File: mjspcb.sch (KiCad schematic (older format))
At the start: 50 parts, among them P1 Batteries, P10 Lipo, P11 grove i2c, P12 grove analog, P13 grove analog, P14 HPMA115S0-XXX, P15 piggyback, P2 serial breakout, P3 I2C breakout, P4 GPS, P5 piezo, P6 BPW34, P7 electrodes, P8 perfboard breakout, P9 reset, Q1 STU60N3LH5, Q2 STU60N3LH5, U1 ATMEGA328P, U2 RFM95W, U3 MCP1700-3302

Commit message: Replace with MJS2020-PROTO2 redesign
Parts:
- removed AE1: Antenna, Connector_PinHeader_2.54mm:PinHeader_1x01_P2.54mm_Vertical, symbol Device:Antenna
- removed C2, C4: 100u, Capacitor_THT:CP_Radial_D5.0mm_P2.00mm, symbol Device:CP
- removed D1: LED, LED_THT:LED_D3.0mm, symbol Device:LED
- removed DC1: 2.7 - 6.0 VDC, Connector_BarrelJack:BarrelJack_Wuerth_6941xx301002, symbol Connector:Barrel_Jack_Switch
- removed H4: MountingHole, MountingHole:MountingHole_3mm, symbol Mechanical:MountingHole
- removed JP1: power select, Connector_PinHeader_2.54mm:PinHeader_1x03_P2.54mm_Vertical, symbol Jumper:Jumper_3_Open
- removed JP2: V1, meetjestad:SolderJumper-3_P1.3mm_Bridged12_RoundedPad1.0x1.5mm_NumberLabels, symbol Jumper:SolderJumper_3_Bridged12
- removed JP3: V2, meetjestad:SolderJumper-3_P1.3mm_Bridged12_RoundedPad1.0x1.5mm_NumberLabels, symbol Jumper:SolderJumper_3_Bridged12
- removed LOGO1: Open source hardware, Symbol:OSHW-Logo_5.7x6mm_SilkScreen, symbol Graphic:Logo_Open_Hardware_Small
- removed LOGO2: MJS Logo, meetjestad:mjs, symbol Graphic:Logo_Open_Hardware_Small
- removed P1: Batteries, Battery:BatteryHolder_Keystone_2479_3xAAA, symbol Connector_Generic:Conn_01x02
- removed P10: Lipo, Connector_JST:JST_PH_S2B-PH-K_1x02_P2.00mm_Horizontal, symbol Connector_Generic:Conn_01x02
- removed P11: grove i2c, Connector:NS-Tech_Grove_1x04_P2mm_Vertical, symbol Connector_Generic:Conn_01x04
- removed P12: grove analog, meetjestad:NS-Tech_Grove_1x04_P2mm_P2.54mm_Vertical, symbol Connector_Generic:Conn_01x04
- removed P13: grove analog, meetjestad:NS-Tech_Grove_1x04_P2mm_P2.54mm_Vertical_Alternative, symbol Connector_Generic:Conn_01x04
- removed P14: HPMA115S0-XXX, Connector_Molex:Molex_PicoBlade_53047-0810_1x08_P1.25mm_Vertical, symbol Connector_Generic:Conn_01x08
- removed P15: piggyback, Connector_PinHeader_2.54mm:PinHeader_1x12_P2.54mm_Vertical, symbol Connector_Generic:Conn_01x12
- removed P2: serial breakout, Connector_PinHeader_2.54mm:PinHeader_1x06_P2.54mm_Vertical, symbol Connector_Generic:Conn_01x06
- removed P3: I2C breakout, meetjestad:Molex_KK-254_44812-0004_1x04_P2.54mm_Vertical, symbol Connector_Generic:Conn_01x04
- removed P4: GPS, Connector_JST:JST_PH_S3B-PH-K_1x03_P2.00mm_Horizontal, symbol Connector_Generic:Conn_01x03
- removed P5: piezo, Connector_Molex:Molex_KK-254_AE-6410-02A_1x02_P2.54mm_Vertical, symbol Connector_Generic:Conn_01x02
- removed P6: BPW34, Connector_Molex:Molex_KK-254_AE-6410-02A_1x02_P2.54mm_Vertical, symbol Connector_Generic:Conn_01x02
- removed P7: electrodes, Connector_Molex:Molex_KK-254_AE-6410-02A_1x02_P2.54mm_Vertical, symbol Connector_Generic:Conn_01x02
- removed P8: perfboard breakout, Connector_PinHeader_2.54mm:PinHeader_1x11_P2.54mm_Vertical, symbol Connector_Generic:Conn_01x11
- removed P9: reset, Connector_PinHeader_2.54mm:PinHeader_1x02_P2.54mm_Vertical, symbol Connector_Generic:Conn_01x02
- removed Q1, Q2: STU60N3LH5, Package_TO_SOT_THT:TO-251-3_Vertical, symbol Device:Q_NMOS_GDS
- removed R1: 10k, Resistor_THT:R_Axial_DIN0207_L6.3mm_D2.5mm_P10.16mm_Horizontal, symbol Device:R
- removed U1: ATMEGA328P, Package_DIP:DIP-28_W7.62mm_Socket, symbol MCU_Microchip_ATmega:ATmega328P-PU
- removed U2: RFM95W, RF_Module:HOPERF_RFM9XW_SMD, symbol RF_AM_FM:RFM95W-868S2
- removed U3: MCP1700-3302, Package_TO_SOT_THT:TO-92_Inline, symbol Regulator_Linear:MCP1700-3302E_TO92
- added C10, C11, C12, C13, C17, C25, C32, C33, C34, C35, C36, C37, C4, C6, C9: 100nF, Capacitor_SMD:C_0805_2012Metric_Pad1.15x1.40mm_HandSolder, symbol Device:C
- added C14, C15, C19, C20, C21, C23, C24, C26, C31, C7: 1uF, Capacitor_SMD:C_0805_2012Metric_Pad1.15x1.40mm_HandSolder, symbol Device:C
- added C16, C18, C22, C27, C28, C29, C30, C8: 4.7uF, Capacitor_SMD:C_0805_2012Metric_Pad1.15x1.40mm_HandSolder, symbol Device:C
- added C2: 12.5pF, Capacitor_SMD:C_0805_2012Metric_Pad1.15x1.40mm_HandSolder, symbol Device:C
- added D1, D2, D3: MBR120VLSFT3G, meetjestad:Diode_SMD-SOD_123, symbol mjspcb-rescue:DIODE-pspice-POC_Rev01-rescue
- added D4: 6,2V, meetjestad:D_SOD-123, symbol Device:D_Zener
- added FB1, FB2, FB3: Ferrite_Bead, Resistor_SMD:R_0805_2012Metric_Pad1.15x1.40mm_HandSolder, symbol mjspcb-rescue:Ferrite_Bead-Device-POC_Rev01-rescue
- added FID1, FID2, FID3: Fiducial, Fiducial:Fiducial_0.5mm_Mask1mm, symbol Mechanical:Fiducial
- added J1: FTDI, Connector_PinHeader_2.54mm:PinHeader_1x06_P2.54mm_Vertical, symbol Connector:Conn_01x06_Male
- added J10: Analog, meetjestad:Grove_4pin&Header_4pin, symbol Connector_Generic:Conn_01x04
- added J11: BOOT0, Connector_PinHeader_2.54mm:PinHeader_1x02_P2.54mm_Vertical, symbol Connector:Conn_01x02_Male
- added J12: Tag connect, meetjestad:Tag connect, symbol Connector:Conn_01x06_Male
- added J13: Conn_Coaxial, meetjestad:SMA connector edge mount, symbol Connector:Conn_Coaxial
- added J14: Lithium Ion, meetjestad:BatteryHolder_18650-PC2, symbol Connector:Conn_01x02_Male
- added J15: Temp/Hum, meetjestad:Grove_4pin&Header_4pin, symbol mjspcb-rescue:Conn_01x04_Male-Connector-POC_Rev01-rescue
- added J16: BPW34, Connector_PinHeader_2.54mm:PinHeader_1x02_P2.54mm_Vertical, symbol Connector:Conn_01x02_Male
- added J17: USB_C_connector, 632723300011_Eagle_WR-USB_rev20b:632723100011, symbol meetjestad:USB_C_connector
- added J18: I2C 3V_perm, meetjestad:Grove_4pin&Header_4pin, symbol Connector_Generic:Conn_01x04
- added J19: I2C 5V_SW, meetjestad:Grove_4pin&Header_4pin, symbol Connector_Generic:Conn_01x04
- added J20: Multi, meetjestad:Grove_4pin&Header_4pin, symbol Connector_Generic:Conn_01x04
- added J3: Prototype header, Connector_PinSocket_2.54mm:PinSocket_1x15_P2.54mm_Vertical, symbol Connector:Conn_01x15_Female
- added J4: Oled, Connector_PinSocket_2.54mm:PinSocket_1x04_P2.54mm_Vertical, symbol mjspcb-rescue:Conn_01x04_Male-Connector-POC_Rev01-rescue
- added J5: Conn_01x02_Male, meetjestad:Battery__holder, symbol Connector:Conn_01x02_Male
- added J6: Solar, Connector_PinHeader_2.54mm:PinHeader_1x02_P2.54mm_Vertical, symbol Connector:Conn_01x02_Male
- added J7: Particulate matter, meetjestad:B5B-ZR, symbol Connector:Conn_01x05_Female
- added J8: Prototype power, Connector_PinSocket_2.54mm:PinSocket_1x06_P2.54mm_Vertical, symbol Connector:Conn_01x06_Female
- added J9: Prototype GND, Connector_PinSocket_2.54mm:PinSocket_1x06_P2.54mm_Vertical, symbol Connector:Conn_01x06_Female
- added L1: 4.7uH, Resistor_SMD:R_0805_2012Metric_Pad1.15x1.40mm_HandSolder, symbol mjspcb-rescue:L-Device-POC_Rev01-rescue
- added LED1: JT-S3030_RGB_LED, meetjestad:JT-S3030_RGB_LED, symbol meetjestad:JT-S3030_RGB_LED
- added Logo_kitt1: Logo_Open_Hardware_Small, meetjestad:Kitt_logo, symbol Graphic:Logo_Open_Hardware_Small
- added Logo_mjs1: Logo_Open_Hardware_Small, meetjestad:mjs_logo, symbol Graphic:Logo_Open_Hardware_Small
- added Logo_mjs2: Logo_Open_Hardware_Small, Symbol:OSHW-Logo2_7.3x6mm_SilkScreen, symbol Graphic:Logo_Open_Hardware_Small
- added PSU1, PSU3, PSU4: TPS7A02, Package_TO_SOT_SMD:SOT-23-5_HandSoldering, symbol mjspcb-rescue:TPS7A02-meetjestad-POC_Rev01-rescue
- added PSU2: XC9140A501MR-G, Package_TO_SOT_SMD:SOT-23-5_HandSoldering, symbol mjspcb-rescue:XC9140A501MR-G-meetjestad-POC_Rev01-rescue
- added Q1, Q2: DMP2035U-7, Package_TO_SOT_SMD:SOT-23, symbol Transistor_FET:DMG2301L
- added R1: 1k, Resistor_SMD:R_0805_2012Metric_Pad1.15x1.40mm_HandSolder, symbol mjspcb-rescue:R-Device-POC_Rev01-rescue
- added R14, R16, R25: 100k, Resistor_SMD:R_0805_2012Metric_Pad1.15x1.40mm_HandSolder, symbol Device:R
- added R15, R20, R21, R28, R29, R30, R31, R32, R33, R39, R40, R43, R44, R45, R46: 10k, Resistor_SMD:R_0805_2012Metric_Pad1.15x1.40mm_HandSolder, symbol Device:R
- added R17, R18, R34, R35, R36, R41, R42: 1k, Resistor_SMD:R_0805_2012Metric_Pad1.15x1.40mm_HandSolder, symbol Device:R
- added R19, R22, R23, R24, R26, R27: 1M, Resistor_SMD:R_0805_2012Metric_Pad1.15x1.40mm_HandSolder, symbol Device:R
- added R37, R38: 100, Resistor_SMD:R_0805_2012Metric_Pad1.15x1.40mm_HandSolder, symbol Device:R
- added SP1, SP2, SP3, SP4, SP5, SP6: SolderJumper_2_Open, Jumper:SolderJumper-2_P1.3mm_Open_TrianglePad1.0x1.5mm, symbol Jumper:SolderJumper_2_Open
- added SW1, SW2: SW_Push, Button_Switch_THT:SW_PUSH_6mm, symbol Switch:SW_Push
- added TP1, TP2, TP3, TP4: TestPoint_Small, TestPoint:TestPoint_Pad_D1.0mm, symbol mjspcb-rescue:TestPoint_Small-Connector-mjspcb-rescue
- added TP5: Sticker field, meetjestad:Sticker field, symbol Connector:TestPoint_Small
- added TP6: Flash OK, meetjestad:Flash OK, symbol Connector:TestPoint_Small
- added TP7: Test OK, meetjestad:Test OK, symbol Connector:TestPoint_Small
- added U1: USBLC-2SC6, Package_TO_SOT_SMD:SOT-23-6_Handsoldering, symbol meetjestad:USBLC-2SC6
- added U2: LoRa_1262_G-NiceRF, meetjestad:LoRa_1262_G-NiceRF, symbol mjspcb-rescue:LoRa_1262_G-NiceRF-meetjestad-POC_Rev01-rescue
- added U3: GPS, meetjestad:GPS_ublox-SAM-M8Q, symbol mjspcb-rescue:ublox_SAM-M8Q-RF_GPS-POC_Rev01-rescue
- added U4: PrototypeGrid, meetjestad:Prototype grid, symbol meetjestad:PrototypeGrid
- added U5: STM32L072RBTx-meetjestad, meetjestad:STM32F072_LQFP-64, symbol mjspcb-rescue:STM32L072RBTx-meetjestad-POC_Rev01-rescue
- added U6: MCP73831, Package_TO_SOT_SMD:SOT-23-5_HandSoldering, symbol meetjestad:MCP73831
- added Y1: 32kHz, Resistor_SMD:R_0805_2012Metric_Pad1.15x1.40mm_HandSolder, symbol mjspcb-rescue:Crystal-Device-POC_Rev01-rescue
- C1: value 100n -> 12.5pF; footprint Capacitor_THT:C_Disc_D3.0mm_W1.6mm_P2.50mm -> Capacitor_SMD:C_0805_2012Metric_Pad1.15x1.40mm_HandSolder
- C3, C5: value 100n -> 100nF; footprint Capacitor_THT:C_Disc_D3.0mm_W1.6mm_P2.50mm -> Capacitor_SMD:C_0805_2012Metric_Pad1.15x1.40mm_HandSolder
- H1, H2, H3: footprint MountingHole:MountingHole_3mm -> meetjestad:Mounting_hole
- R10: value 1k -> 100k; footprint Resistor_THT:R_Axial_DIN0207_L6.3mm_D2.5mm_P10.16mm_Horizontal -> Resistor_SMD:R_0805_2012Metric_Pad1.15x1.40mm_HandSolder
- R11: value 10k -> 100k; footprint Resistor_THT:R_Axial_DIN0207_L6.3mm_D2.5mm_P10.16mm_Horizontal -> Resistor_SMD:R_0805_2012Metric_Pad1.15x1.40mm_HandSolder
- R12: value 100k -> 1k; footprint Resistor_THT:R_Axial_DIN0207_L6.3mm_D2.5mm_P10.16mm_Horizontal -> Resistor_SMD:R_0805_2012Metric_Pad1.15x1.40mm_HandSolder
- R13, R6, R7: footprint Resistor_THT:R_Axial_DIN0207_L6.3mm_D2.5mm_P10.16mm_Horizontal -> Resistor_SMD:R_0805_2012Metric_Pad1.15x1.40mm_HandSolder
- R2, R9: value 10k -> 1k; footprint Resistor_THT:R_Axial_DIN0207_L6.3mm_D2.5mm_P10.16mm_Horizontal -> Resistor_SMD:R_0805_2012Metric_Pad1.15x1.40mm_HandSolder
- R3, R4, R5, R8: value 1k -> 10k; footprint Resistor_THT:R_Axial_DIN0207_L6.3mm_D2.5mm_P10.16mm_Horizontal -> Resistor_SMD:R_0805_2012Metric_Pad1.15x1.40mm_HandSolder
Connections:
- net labels added: 3V-perm_CPU, 3V-sw_GPS, 3V-sw_sens, 5V-sw, BOOT0, NRST, PA0, PA1, PA10, PA11, PA12, PA13, PA14, PA15, PA2, PA3, PA4, PA5, PA6, PA7, PA8, PA9, PB0, PB1, PB10, PB11, PB12, PB13, PB14, PB15, PB2, PB3, PB4, PB5, PB6, PB7, PB8, PB9, PC0, PC1, PC10, PC11, PC2, PC3, PC4, PC5, PC6, PC7, PC8, PC9, PH0, PH1, Solar, VBUS, Vin
- net labels removed: -BATT, 5V, A0, A1, A2, A3, D10, D2, D3, D4, D5, D6, D7, D8, D9, MISO, MOSI, RST, RXD, SCK, SCL, SDA, SW_GND, TXD, VCC, VIN, X1, X2
- wire segments 203 -> 500
- no-connect marks 8 -> 0
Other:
- note added: "1% precision\n"
- note added: "ADC4"
- note added: "ADC5\n"
- note added: "ADC_IN0 / Dx\n"
- note added: "ADC_IN1 / Dx"
- note added: "ADC_IN4 / DAC_OUT1"
- note added: "ADC_IN5 / DAC_OUT2"
- note added: "ADC_IN8 / VREF_OUT\n"
- note added: "Battery voltage: 0V - 6V\nPC4 Voltage: 0V - 3V"
- note added: "Board ID\n"
- note added: "C1 and C2: High-quality external ceramic capacitors"
- note added: "Ceramic, 10V\n"
- note added: "Charge status\nTri-state logic output\n\n"
- note added: "Close for I2C communication"
- note added: "Crystal: ABS06-32.768KHZ-1-T\n"
- note added: "DNP\n"
- note added: "Dx"
- note added: "GND: I2C, floating: UART"
- note added: "Grove connectoren\n"
- note added: "H: Active\nL: Stand-by\n"
- note added: "I2C 3V_perm sensors"
- note added: "I2C 5V_SW sensors"
- note added: "I2C1_SCL"
- note added: "I2C1_SCL 3V perm\n"
- note added: "I2C1_SDA"
- note added: "I2C1_SDA 3V perm\n"
- note added: "I2C2_SCL"
- note added: "I2C2_SCL 5V_SW"
- note added: "I2C2_SDA"
- note added: "I2C2_SDA 5V_SW"
- note added: "Ireg = 200mA"
- note added: "Logo KITT\n"
- note added: "Logo mjs"
- note added: "Logo open hardware"
- note added: "Microcontroller\n"
- note added: "POWER\n"
- note added: "Prototype\n"
- note added: "SPI1_MISO"
- note added: "SPI1_MOSI 3V perm"
- note added: "SPI1_NSS\n"
- note added: "SPI1_SCK\n"
- note added: "SPI2_MISO / I2C2_SDA / I2S2_MCK"
- note added: "SPI2_MOSI / I2S2_SD"
- note added: "SPI2_NSS / I2C2_SMBA / I2S2_WS\n"
- note added: "SPI2_SCK / I2C2_SCL / I2S2_CK\n"
- note added: "SWCLK\n"
- note added: "SWDIO\n"
- note added: "Sensors"
- note added: "Threshold voltage: -0.7 V\n"
- note added: "USART1_RX"
- note added: "USART1_TX\n"
- note added: "USART2_RX\n"
- note added: "USART2_TX"
- note added: "USB_DM\n"
- note added: "USB_DP\n"
- note added: "Vout = 2V\n"
- note added: "filter\n"
- note added: "ground plane on top layer\n"
- note added: "pair 100 ohm\n"
- note removed: "!! 5V for HPMA !!"
- note removed: "!! 5V for SDS011 !!"
- note removed: "A1 shared with P7"
- note removed: "Air temperature and humidity sensor"
- note removed: "D6/D7 shared with P7"
- note removed: "Disdrometer"
- note removed: "GPS module"
- note removed: "Intended for softserial"
- note removed: "Other sensors"
- note removed: "PAR meter"
- note removed: "Soil moisture sensor"
- note removed: "aquatictechtank.net/viewtopic.php?f=11&t=150"
- note removed: "core schematic"
- note removed: "forum.arduino.cc/index.php?topic=37975"
- note removed: "optional sensors"
- note removed: "power & programming"
- note removed: "rx"
- note removed: "rx/tx viewed from MCU"
- note removed: "standard sensors"
- note removed: "tx"
- note removed: "www.hoperf.nl/RFM95W"
- note removed: "www.sparkfun.com/products/13740"
- note removed: "www.sparkfun.com/products/13763"

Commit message: Update to MJS2020-PROTO3
See CHANGELOG.md for detailed changes.
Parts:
- removed J11: BOOT0, Connector_PinHeader_2.54mm:PinHeader_1x02_P2.54mm_Vertical, symbol Connector:Conn_01x02_Male
- removed J3: Prototype header, Connector_PinSocket_2.54mm:PinSocket_1x15_P2.54mm_Vertical, symbol Connector:Conn_01x15_Female
- removed LED1: JT-S3030_RGB_LED, meetjestad:JT-S3030_RGB_LED, symbol meetjestad:JT-S3030_RGB_LED
- removed R1: 1k, Resistor_SMD:R_0805_2012Metric_Pad1.15x1.40mm_HandSolder, symbol mjspcb-rescue:R-Device-POC_Rev01-rescue
- removed SP3, SP4, SP5, SP6: SolderJumper_2_Open, Jumper:SolderJumper-2_P1.3mm_Open_TrianglePad1.0x1.5mm, symbol Jumper:SolderJumper_2_Open
- removed TP1, TP2, TP3, TP4: TestPoint_Small, TestPoint:TestPoint_Pad_D1.0mm, symbol mjspcb-rescue:TestPoint_Small-Connector-mjspcb-rescue
- added C38, C39, C40: 100nF, Capacitor_SMD:C_0805_2012Metric_Pad1.15x1.40mm_HandSolder, symbol mjspcb-rescue:C-Device-POC_Rev01-rescue
- added D5: LED, LED_SMD:LED_0805_2012Metric, symbol Device:LED
- added D6: LED_RGB, meetjestad:JTS3535, symbol Device:LED_RGB
- added J2: Conn_01x16_Female, Connector_PinSocket_2.54mm:PinSocket_1x16_P2.54mm_Vertical, symbol Connector:Conn_01x16_Female
- added J3: Conn_01x02_Male, Connector_PinHeader_2.54mm:PinHeader_1x02_P2.54mm_Vertical, symbol Connector:Conn_01x02_Male
- added Logo_mjs3: Logo_Open_Hardware_Small, meetjestad:mjs-logo-22mm, symbol Graphic:Logo_Open_Hardware_Small
- added Logo_mjs4: Logo_Open_Hardware_Small, Symbol:OSHW-Logo2_7.3x6mm_SilkScreen, symbol Graphic:Logo_Open_Hardware_Small
- added R1: 1k, Resistor_SMD:R_0805_2012Metric_Pad1.15x1.40mm_HandSolder, symbol Device:R
- added R47: 1M, Resistor_SMD:R_0805_2012Metric_Pad1.15x1.40mm_HandSolder, symbol Device:R
- added R48, R49, R50: 10k, Resistor_SMD:R_0805_2012Metric_Pad1.15x1.40mm_HandSolder, symbol Device:R
- added SW3: SW_Push, meetjestad:Switch_Header2.54_Combi, symbol Switch:SW_Push
- added U7: MCP9808_MSOP, Package_SO:MSOP-8_3x3mm_P0.65mm, symbol Sensor_Temperature:MCP9804_MSOP
- added U8: SST26VF032B, Package_SO:SOIJ-8_5.3x5.3mm_P1.27mm, symbol meetjestad:SST26VF032B
- C1, C10, C11, C12, C13, C14, C15, C16, C17, C18, C19, C2, C20, C21, C22, C23, C24, C25, C26, C27, C28, C29, C3, C30, C31, C32, C33, C34, C35, C36, C37, C4, C5, C6, C7, C8, C9: symbol Device:C -> mjspcb-rescue:C-Device-POC_Rev01-rescue
- H1, H2, H3: footprint meetjestad:Mounting_hole -> MountingHole:MountingHole_3.2mm_M3
- J10, J18, J19, J20: footprint meetjestad:Grove_4pin&Header_4pin -> meetjestad:2,54_2.0pitchCombi
- J12: value Tag connect -> SWD; footprint meetjestad:Tag connect -> Connector_PinHeader_2.54mm:PinHeader_1x06_P2.54mm_Vertical
- J14: footprint meetjestad:BatteryHolder_18650-PC2 -> meetjestad:Combi_2.0_2.45pitch_2PIN
- J15: footprint meetjestad:Grove_4pin&Header_4pin -> meetjestad:SI7021
- J17: footprint 632723300011_Eagle_WR-USB_rev20b:632723100011 -> meetjestad:USB-C_new
- J4: footprint Connector_PinSocket_2.54mm:PinSocket_1x04_P2.54mm_Vertical -> meetjestad:OLED_1.3
- J6: footprint Connector_PinHeader_2.54mm:PinHeader_1x02_P2.54mm_Vertical -> meetjestad:Combi_2.0_2.45pitch_2PIN
- Logo_mjs1: footprint meetjestad:mjs_logo -> meetjestad:mjs-logo-16mm
- R15: value 10k -> 3k3
- R24: value 1M -> 100k
- R25: value 100k -> 10k
- R34, R35, R36: value 1k -> 3k3
- R43, R44, R45: value 10k -> 1k
- R46: value 10k -> 1M
- SP2: footprint Jumper:SolderJumper-2_P1.3mm_Open_TrianglePad1.0x1.5mm -> Jumper:SolderJumper-2_P1.3mm_Bridged_RoundedPad1.0x1.5mm
- U5: value STM32L072RBTx-meetjestad -> STM32L072RZTx-meetjestad
- e1: renamed from SP1; footprint Jumper:SolderJumper-2_P1.3mm_Open_TrianglePad1.0x1.5mm -> Jumper:SolderJumper-2_P1.3mm_Bridged_RoundedPad1.0x1.5mm
- renumbered PSU3 to PSU1, PSU1 to PSU2, PSU4 to PSU3, PSU2 to PSU4
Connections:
- net labels added: PC12, PC13
- wire segments 500 -> 517
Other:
- note added: "Address: 0011000"
- note added: "Logo mjs 16mm\n"
- note added: "Logo mjs 22mm\n"
- note added: "VBUS: 0V - 6V\nPA7 Voltage: 0V - 3V"
- note removed: "ADC_IN0 / Dx\n"
- note removed: "Board ID\n"
- note removed: "Charge status\nTri-state logic output\n\n"
- note removed: "Logo mjs"
- note removed: "Vout = 2V\n"
- moved on the sheet: C10, C18, C27, C4, C6, C7, C8, D4, FB1, J13, R22, R23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

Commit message: Update to MJS2020-PROTO4
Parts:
- removed J17: USB_C_connector, meetjestad:USB-C_new, symbol meetjestad:USB_C_connector
- added J11: USBC(2.0), meetjestad:DX07S016JA3R1500, symbol mjspcb-rescue:USBC(2.0)-meetjestad
- H1, H2, H3: footprint MountingHole:MountingHole_3.2mm_M3 -> meetjestad:MountingHole_3.2mm_M3
- J15: footprint meetjestad:SI7021 -> meetjestad2:SI7021
- J16, J3: footprint Connector_PinHeader_2.54mm:PinHeader_1x02_P2.54mm_Vertical -> meetjestad:PinHeader_Male_1X2
- J2: footprint Connector_PinSocket_2.54mm:PinSocket_1x16_P2.54mm_Vertical -> meetjestad:PinHeader_Female_1X16
- J5: footprint meetjestad:Battery__holder -> meetjestad2:Battery__holder
- J8, J9: footprint Connector_PinSocket_2.54mm:PinSocket_1x06_P2.54mm_Vertical -> meetjestad:PinHeader_Female_1X6
- SW1, SW2: footprint Button_Switch_THT:SW_PUSH_6mm -> meetjestad:SW_Push_6mm
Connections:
- net GND: now also J11.1 (GND), J11.12 (GND), J11.S (GND)
- net VBUS: now also J11.11 (VBUS), J11.2 (VBUS)
- net at R29.1, R30.1: now also J11.3 (CC1)
- net at R31.2, R32.2: now also J11.9 (CC2)
- net at U1.3 (I/O2): now also J11.6 (D+), J11.7 (D+)
- net at U1.1 (I/O1): now also J11.5 (D-), J11.8 (D-)
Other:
- moved on the sheet: C25, C26, R29, R30, R31, R32, U1

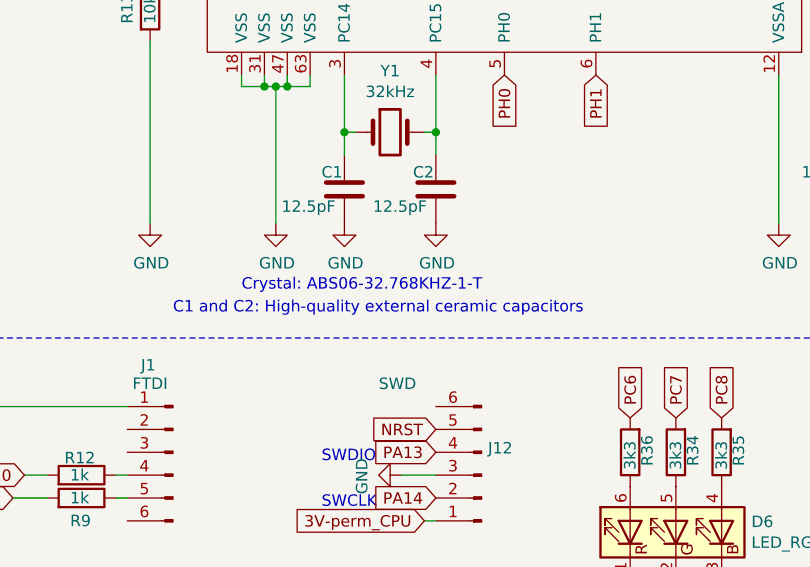
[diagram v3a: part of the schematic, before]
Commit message: Update crystal and load caps
Turns out the type number in the schematic was not actually used, but
the ABS06-32.768KHZ-7 was used instead (which better matches the load
capacitors chosen).
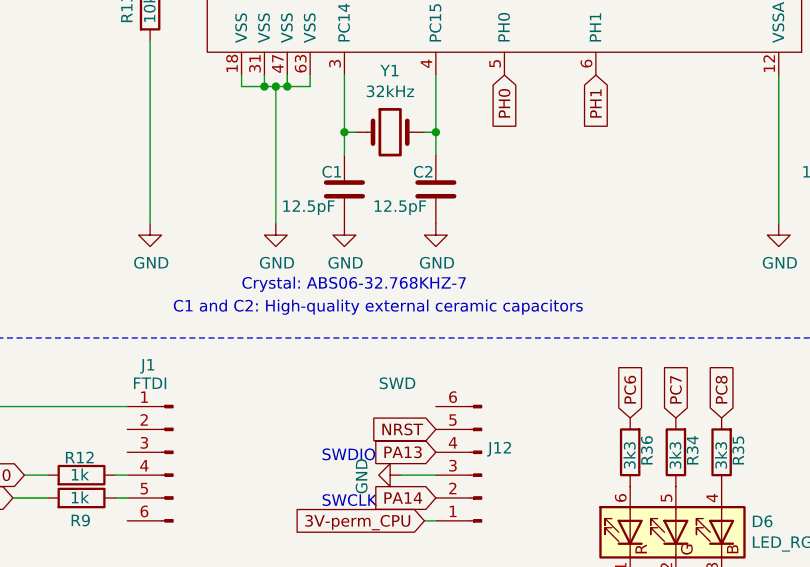
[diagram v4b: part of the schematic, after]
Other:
- note added: "Crystal: ABS06-32.768KHZ-7\n"
- note removed: "Crystal: ABS06-32.768KHZ-1-T\n"
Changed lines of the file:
@@
 3V-perm_CPU
 Text Notes 2550 6750 0    50   ~ 0
-Crystal: ABS06-32.768KHZ-1-T\n
+Crystal: ABS06-32.768KHZ-7\n
 Text GLabel 1550 7650 0    50   Input ~ 0
 PA9
